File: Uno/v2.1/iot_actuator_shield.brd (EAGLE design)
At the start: 100 x 80 mm, 6 parts, among them IC1 REG1117, U1 ARDUINOR3-DIMENSION

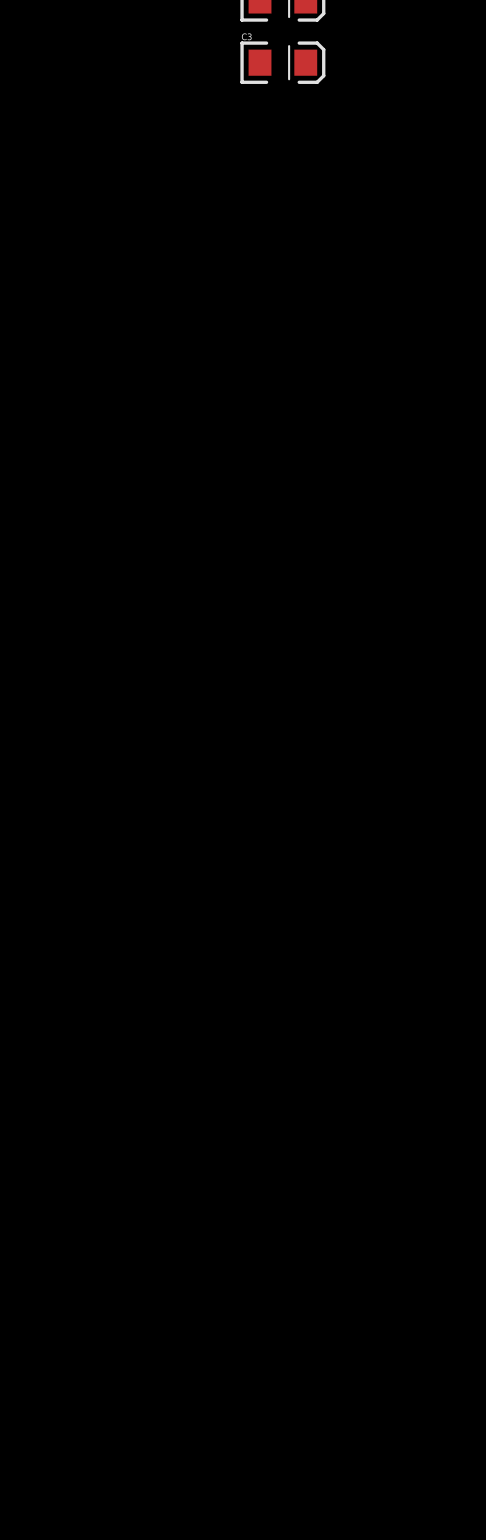
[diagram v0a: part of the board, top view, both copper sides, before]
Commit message: IO-Expander and Darlington array
the output circuitry is added to schematics (copied
from the ThermoShield project)
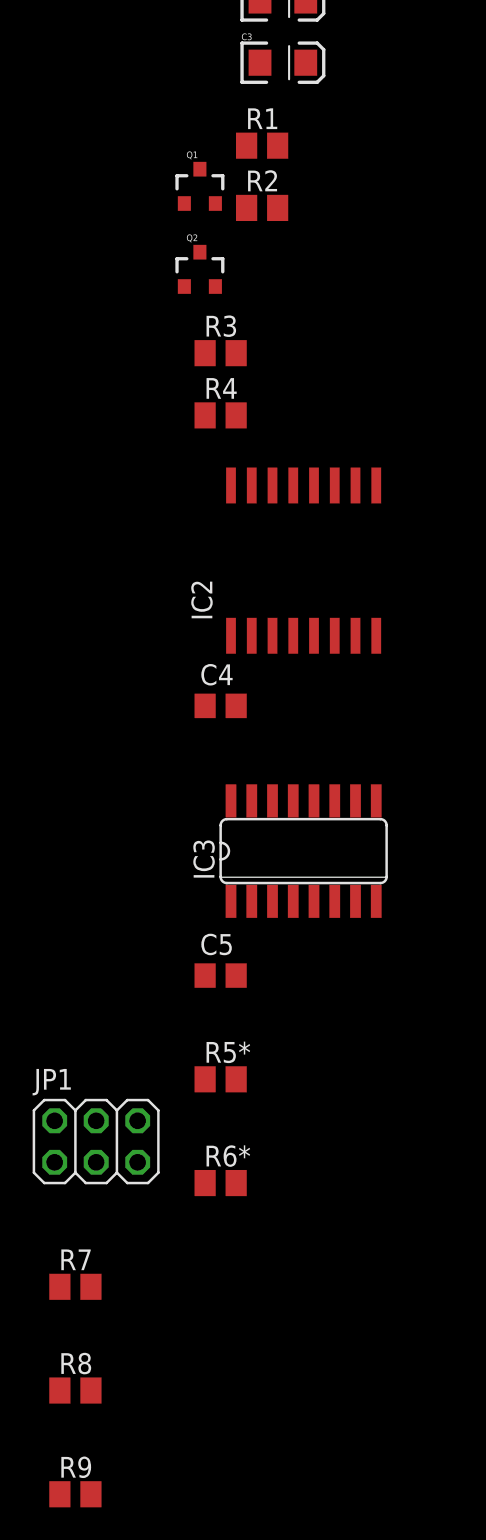
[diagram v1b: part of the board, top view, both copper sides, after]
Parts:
- added C4, C5: 100nF, rcl:C0805
- added IC2: PCF8574T, micro-philips:SO16W
- added IC3: ULN2003AD, uln-udn:SO16
- added JP1: (no value), pinhead:2X03
- added Q1, Q2: 200mA/50V, SparkFun-DiscreteSemi:SOT23-3
- added R1, R2, R3, R4: 10K, resistor:M0805
- added R5*, R6*, R7, R8, R9: 4K7, resistor:M0805
- C2, C3: value (none) -> 5uF
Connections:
- new net AO0: IC3.16
- new net AO1: IC3.15
- new net AO2: IC3.14
- new net AO3: IC3.13
- new net AO4: IC3.12
- new net AO5: IC3.11
- new net AO6: IC3.10
- new net AO7: IC2.12
- new net N$1: Q2.2, R3.1, U$1.RXD
- new net N$10: IC2.1, JP1.2, R7.2
- new net N$11: IC2.2, JP1.4, R8.2
- new net N$12: IC2.3, JP1.6, R9.2
- new net N$2: Q1.2, R1.1, U$1.TXD
- new net N$3: IC2.4, IC3.1
- new net N$4: IC2.5, IC3.2
- new net N$5: IC2.6, IC3.3
- new net N$6: IC2.7, IC3.4
- new net N$7: IC2.9, IC3.5
- new net N$8: IC2.10, IC3.6
- new net N$9: IC2.11, IC3.7
- new net RX: Q1.3, R2.1
- new net SCL: IC2.14, R6*.1
- new net SDA: IC2.15, R5*.1
- new net TX: Q2.3, R4.1
- net 3V3: now also Q1.1, Q2.1, R1.2, R3.2
- net GND: now also C4.2, C5.2, IC2.8, IC3.8, R7.1, R8.1, R9.1
- net VDD: now also C4.1, C5.1, IC2.16, IC3.9, JP1.1, JP1.3, JP1.5, R2.2, R4.2, R5*.2, R6*.2

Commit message: shield added
most components added including the shield
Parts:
- removed C2, C3: 5uF, SparkFun-Capacitors:EIA3216
- removed C4, C5: 100nF, rcl:C0805
- removed R1, R2, R3, R4: 10K, resistor:M0805
- removed R5*, R6*: 4K7, resistor:M0805
- removed U$1: ESP8266-07, lio:ESP-07
- added 1, 2, 3, 4, 5, 6, 7, 8: (no value), led:CHIP-LED0805
- added ANALOG: (no value), pinhead:1X06
- added C10, C13, C14, C9: 100nF, rcl:C0805
- added C11, C12, C8: 5uF, SparkFun-Capacitors:EIA3216
- added FRAME1, FRAME2: FRAME-LETTER, SparkFun-Aesthetics:CREATIVE_COMMONS
- added J1, J2: (no value), SmartPrj:1X08-TH
- added J3: (no value), SmartPrj:1X10-TH
- added JP5: (no value), pinhead:2X03
- added LED9: Blue, led:CHIP-LED0805
- added MISHA1: ESP8266-07, lio:ESP-07
- added R10, R11, R12, R14, R15, R16, R22: 3K3, rcl:R0805
- added R13: 1K, rcl:R1206
- added R23, R24, R25, R26: 10K, rcl:R0805
- added R5, R6: 1K, rcl:R0805
- added R8*, R9*: 4K7, rcl:R0805
- added U2: AD5165BUJZ100-R2, AD5165_DigitalPot:UJ_8
- added X1: (no value), con-phoenix-500:MSTBV8
- added X10, X11, X2, X3, X4, X5, X6, X7, X8, X9: (no value), con-phoenix-500:MSTBV2
- C1: value (none) -> 100nF
- IC1: value REG1117 -> PCF8574T; device burr-brown:SOT223 -> micro-philips:SO16W
- IC2: value PCF8574T -> ULN2003AD; device micro-philips:SO16W -> uln-udn:SO16
- IC3: value ULN2003AD -> REG1117; device uln-udn:SO16 -> burr-brown:SOT223
- JP1: device pinhead:2X03 -> pinhead:2X04
- R7: value 4K7 -> 1K; device resistor:M0805 -> rcl:R0805
- R8, R9: value 4K7 -> 3K3; device resistor:M0805 -> rcl:R0805
- U1: value ARDUINOR3-DIMENSION -> CD74HCT4051_D_16; device adafruit:ARDUINOR3 -> misha-74HCT4051:D16
- moved C1 155.1 mm to (34.3, -127.8)
- moved U1 154.2 mm to (-2.54, -131.3)
- moved IC3 149.3 mm to (15.4, 30.6), turned to 270 degrees
- moved R9 137.2 mm to (35.2, -139.4)
- moved R8 133.5 mm to (30.2, -139.4)
- moved JP1 114.8 mm to (-0.89, -156.0)
- moved R7 105.8 mm to (3.68, -86.1)
- moved Q2 101.6 mm to (8.64, -50.2)
- moved IC1 99.9 mm to (0.76, -63.0)
- moved Q1 98.4 mm to (4.95, -50.2)
- moved IC2 87.8 mm to (0.64, -72.9)
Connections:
- removed net 3V: U1.3V
- removed net 5V: U1.5V
- removed net GND1: U1.GND1
- removed net GND2: U1.GND2
- removed net N$12: IC2.3, JP1.6, R9.2
- removed net VIN: U1.VIN
- new net A0: ANALOG.1, JP1.1
- new net A1: ANALOG.2, JP1.3
- new net A2: ANALOG.3, JP1.5
- new net A3: ANALOG.4, JP1.7
- new net AS0: U1.13, X4.1
- new net AS1: U1.14, X5.1
- new net AS2: U1.15, X6.1
- new net AS3: U1.12, X7.1
- new net AS4: U1.1, X8.1
- new net AS5: U1.5, X9.1
- new net AS6: U1.2, X10.1
- new net AS7: U1.4, X11.1
- new net D10: U1.9
- new net D11: U2.6
- new net D51(MOSI): U2.5
- new net D52(SCLK): U2.4
- new net D8: U1.11
- new net D9: U1.10
- new net N$126: LED9.A, R22.1
- new net N$23: 2.A, R9.1
- new net N$24: IC1.2, JP5.4, R6.1
- new net N$25: IC1.3, JP5.6, R7.1
- new net N$32: 3.A, R10.1
- new net N$36: C8.A, R13.1
- new net N$40: MISHA1.TXD, Q1.2, R23.1
- new net N$41: MISHA1.RXD, Q2.2, R24.1
- new net N$46: 4.A, R11.1
- new net N$47: 5.A, R12.1
- new net N$48: 6.A, R14.1
- new net N$49: 7.A, R15.1
- new net N$50: 8.A, R16.1
- net 3V3: now also C12.A, C13.1, IC3.2, MISHA1.CH_PD, MISHA1.REST, MISHA1.VCC, R23.2, R24.2; no longer C1.1, C3.A, IC1.2, R1.2, R3.2, U$1.CH_PD, U$1.REST, U$1.VCC
- net AO0: now also 1.C, IC2.16, X1.1; no longer IC3.16
- net AO1: now also 2.C, IC2.15, X1.2; no longer IC3.15
- net AO2: now also 3.C, IC2.14, X1.3; no longer IC3.14
- net AO3: now also 4.C, IC2.13, X1.4; no longer IC3.13
- net AO4: now also 5.C, IC2.12, X1.5; no longer IC3.12
- net AO5: now also 6.C, IC2.11, X1.6; no longer IC3.11
- net AO6: now also 7.C, IC2.10, X1.7; no longer IC3.10
- net AO7: now also 8.C, IC1.12, X1.8; no longer IC2.12
- net GND: now also C10.2, C11.C, C12.C, C13.2, C14.2, C8.C, C9.2, IC1.8, IC3.1, JP5.1, JP5.3, JP5.5, LED9.C, MISHA1.GND, MISHA1.GPIO15, U1.6, U1.7, U1.8, U2.3, X10.2, X11.2, X3.1, X3.2, X4.2, X5.2, X6.2, X7.2, X8.2, X9.2; no longer C2.C, C3.C, C4.2, C5.2, IC1.1, IC3.8, R7.1, R8.1, R9.1, U$1.GND, U$1.GPIO15, U1.GND
- net N$1: now also JP1.2, JP1.4, JP1.6, JP1.8; no longer Q2.2, R3.1, U$1.RXD
- net N$10: now also IC1.1, JP5.2, R5.1; no longer IC2.1, JP1.2, R7.2
- net N$11: now also 1.A, R8.1; no longer IC2.2, JP1.4, R8.2
- net N$2: now also R13.2, U1.3, U2.1; no longer Q1.2, R1.1, U$1.TXD
- net N$3: now also IC1.4, IC2.1; no longer IC2.4, IC3.1
- net N$4: now also IC1.5, IC2.2; no longer IC2.5, IC3.2
- net N$5: now also IC1.6, IC2.3; no longer IC2.6, IC3.3
- net N$6: now also IC1.7, IC2.4; no longer IC2.7, IC3.4
- net N$7: now also IC1.9, IC2.5; no longer IC2.9, IC3.5
- net N$8: now also IC1.10, IC2.6; no longer IC2.10, IC3.6
- net N$9: now also IC1.11, IC2.7; no longer IC2.11, IC3.7
- net RX: now also J1.1, R25.1; no longer R2.1
- net SCL: now also ANALOG.6, IC1.14, R9*.1; no longer IC2.14, R6*.1
- net SDA: now also ANALOG.5, IC1.15, R8*.1; no longer IC2.15, R5*.1
- net TX: now also J1.2, R26.1; no longer R4.1
- net VDD: now also C1.1, C10.1, C11.A, C14.1, C9.1, IC1.16, IC2.9, IC3.3, R10.2, R11.2, R12.2, R14.2, R15.2, R16.2, R22.2, R25.2, R26.2, R5.2, R6.2, R7.2, R8*.2, R8.2, R9*.2, R9.2, U1.16, U2.2, U2.8, X2.1, X2.2; no longer C2.A, C4.1, C5.1, IC1.3, IC2.16, IC3.9, JP1.1, JP1.3, JP1.5, R2.2, R4.2, R5*.2, R6*.2
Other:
- board size 100 x 80 mm -> 86.1 x 80.2 mm
- board text added: "0"
- board text added: "0 1 2 3 4 5"
- board text added: "1"
- board text added: "10"
- board text added: "11"
- board text added: "12"
- board text added: "13"
- board text added: "2"
- board text added: "3"
- board text added: "3V3"
- board text added: "4"
- board text added: "5"
- board text added: "5V Gnd 9V"
- board text added: "6"
- board text added: "7"
- board text added: "8"
- board text added: "9"
- board text added: "AREF"
- board text added: "DIGITAL"
- board text added: "ETH"
- board text added: "GND"
- board text added: "RES"
- board text added: "SCL"
- board text added: "SDA"
- board text added: "USB"
